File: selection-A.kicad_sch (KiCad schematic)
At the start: 3 parts, among them U0 SN74LS08N, U10 SN74LS08N, U13 SN74LVC1G32DBVR

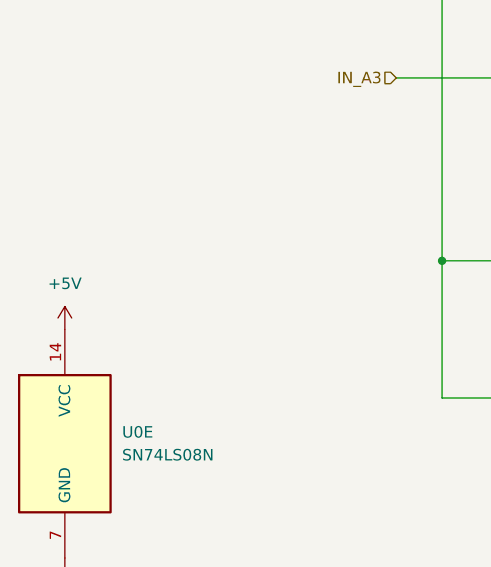
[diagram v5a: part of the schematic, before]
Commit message: feat: added capacitor with footprint
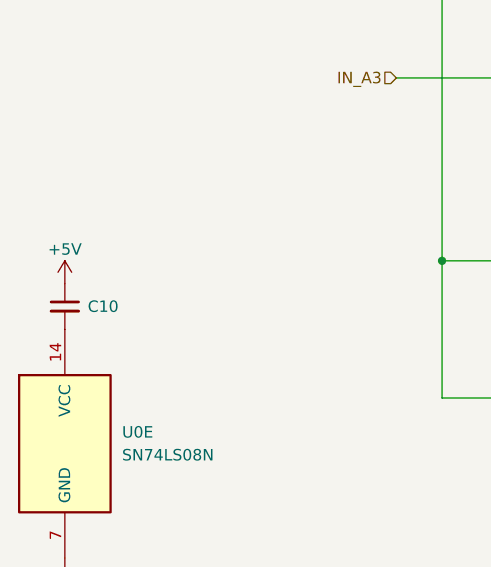
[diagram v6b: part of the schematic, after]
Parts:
- added C10: C_Small, Capacitor_SMD:C_0603_1608Metric_Pad1.08x0.95mm_HandSolder, symbol Device:C_Small
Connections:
- net +5V: now also C10.1; no longer U0.14 (VCC)
- new net: C10.2, U0.14 (VCC)
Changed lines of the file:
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@@
+	)
+	(symbol
+		(lib_id "Device:C_Small")
+		(at 54.61 127 0)
+		(unit 1)
+		(body_style 1)
+		(exclude_from_sim no)
+		(in_bom yes)
+		(on_board yes)
+		(in_pos_files yes)
+		(dnp no)
+		(fields_autoplaced yes)
+		(property "Reference" "C10"
+			(at 57.15 127.0062 0)
+			(show_name no)
+			(do_not_autoplace no)
+			(effects
+				(font
+					(size 1.27 1.27)
+				)
+				(justify left)
+			)
+		)
+		(property "Value" "C_Small"
+			(at 57.15 128.2762 0)
+			(hide yes)
+			(show_name no)
+			(do_not_autoplace no)
+			(effects
+				(font
+					(size 1.27 1.27)
+				)
+				(justify left)
+			)
+		)
+		(property "Footprint" "Capacitor_SMD:C_0603_1608Metric_Pad1.08x0.95mm_HandSolder"
+			(at 54.61 127 0)
+			(hide yes)
+			(show_name no)
+			(do_not_autoplace no)
+			(effects
+				(font
+					(size 1.27 1.27)
+				)
+			)
+		)
+		(property "Datasheet" ""
+			(at 54.61 127 0)
+			(hide yes)
+			(show_name no)
+			(do_not_autoplace no)
+			(effects
+				(font
+					(size 1.27 1.27)
+				)
+			)
+		)
+		(property "Description" "Unpolarized capacitor, small symbol"
+			(at 54.61 127 0)
+			(hide yes)
+			(show_name no)
+			(do_not_autoplace no)
+			(effects
+				(font
+					(size 1.27 1.27)
+				)
+			)
+		)
+		(pin "2"
+		)
+		(pin "1"
+		)
+		(instances
+			(project "alu"
+				(path "/4987240f-8890-46b8-b8e9-0d60580cb205/30c1ae8d-c878-40aa-ace0-371f489a4d3c"
+					(reference "C10")
+					(unit 1)
+				)
+			)
+		)
 	)
 	(symbol
@@
 	)
 	(symbol
+		(lib_id "power:+5V")
+		(at 54.61 124.46 0)
+		(unit 1)
+		(body_style 1)
+		(exclude_from_sim no)
+		(in_bom yes)
+		(on_board yes)
+		(in_pos_files yes)
+		(dnp no)
+		(property "Reference" "#PWR040"
+			(at 54.61 128.27 0)
+			(hide yes)
+			(show_name no)
+			(do_not_autoplace no)
+			(effects
+				(font
+					(size 1.27 1.27)
+				)
+			)
+		)
+		(property "Value" "+5V"
+			(at 54.61 120.65 0)
+			(show_name no)
+			(do_not_autoplace no)
+			(effects
+				(font
+					(size 1.27 1.27)
+				)
+			)
+		)
+		(property "Footprint" ""
+			(at 54.61 124.46 0)
+			(hide yes)
+			(show_name no)
+			(do_not_autoplace no)
+			(effects
+				(font
+					(size 1.27 1.27)
+				)
+			)
+		)
+		(property "Datasheet" ""
+			(at 54.61 124.46 0)
+			(hide yes)
+			(show_name no)
+			(do_not_autoplace no)
+			(effects
+				(font
+					(size 1.27 1.27)
+				)
+			)
+		)
+		(property "Description" "Power symbol creates a global label with name \"+5V\""
+			(at 54.61 124.46 0)
+			(hide yes)
+			(show_name no)
+			(do_not_autoplace no)
+			(effects
+				(font
+					(size 1.27 1.27)
+				)
+			)
+		)
+		(pin "1"
+		)
+		(instances
+			(project "alu"
+				(path "/4987240f-8890-46b8-b8e9-0d60580cb205/30c1ae8d-c878-40aa-ace0-371f489a4d3c"
+					(reference "#PWR040")
+					(unit 1)
+				)
+			)
+		)
+	)
+	(symbol
 		(lib_id "74xx:74LS08")
 		(at 54.61 142.24 0)
@@
 				)
 			)
-		)
-	)
-	(symbol
-		(lib_id "power:+5V")
-		(at 54.61 129.54 0)
-		(unit 1)
-		(body_style 1)
-		(exclude_from_sim no)
-		(in_bom yes)
-		(on_board yes)
-		(in_pos_files yes)
-		(dnp no)
-		(fields_autoplaced yes)
-		(property "Reference" "#PWR05"
-			(at 54.61 133.35 0)
-			(hide yes)
-			(show_name no)
-			(do_not_autoplace no)
-			(effects
-				(font
-					(size 1.27 1.27)
-				)
-			)
-		)
-		(property "Value" "+5V"
-			(at 54.61 124.46 0)
-			(show_name no)
-			(do_not_autoplace no)
-			(effects
-				(font
-					(size 1.27 1.27)
-				)
-			)
-		)
-		(property "Footprint" ""
-			(at 54.61 129.54 0)
-			(hide yes)
-			(show_name no)
-			(do_not_autoplace no)
-			(effects
-				(font
-					(size 1.27 1.27)
-				)
-			)
-		)
-		(property "Datasheet" ""
-			(at 54.61 129.54 0)
-			(hide yes)
-			(show_name no)
-			(do_not_autoplace no)
-			(effects
-				(font
-					(size 1.27 1.27)
-				)
-			)
-		)
-		(property "Description" "Power symbol creates a global label with name \"+5V\""
-			(at 54.61 129.54 0)
-			(hide yes)
-			(show_name no)
-			(do_not_autoplace no)
-			(effects
-				(font
-					(size 1.27 1.27)
-				)
-			)
-		)
-		(pin "1"
-		)
-		(instances
-			(project "alu"
-				(path "/4987240f-8890-46b8-b8e9-0d60580cb205/30c1ae8d-c878-40aa-ace0-371f489a4d3c"
-					(reference "#PWR05")
-					(unit 1)
-				)
-			)

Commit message: fix: merge
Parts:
- renumbered U13 to U10, U0 to U7, U10 to U9, U0 to U9
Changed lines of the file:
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@@
 		(dnp no)
 		(fields_autoplaced yes)
-		(property "Reference" "U13"
+		(property "Reference" "U10"
 			(at 124.46 34.2198 0)
 			(show_name no)
@@
 			(project "alu"
 				(path "/4987240f-8890-46b8-b8e9-0d60580cb205/30c1ae8d-c878-40aa-ace0-371f489a4d3c"
-					(reference "U13")
+					(reference "U10")
 					(unit 1)
 				)
@@
 		(dnp no)
 		(fields_autoplaced yes)
-		(property "Reference" "U0"
+		(property "Reference" "U7"
 			(at 135.8817 67.31 0)
 			(show_name no)
@@
 			(project "alu"
 				(path "/4987240f-8890-46b8-b8e9-0d60580cb205/30c1ae8d-c878-40aa-ace0-371f489a4d3c"
-					(reference "U0")
+					(reference "U7")
 					(unit 2)
 				)
@@
 		(dnp no)
 		(fields_autoplaced yes)
-		(property "Reference" "U10"
+		(property "Reference" "U9"
 			(at 135.8817 110.49 0)
 			(show_name no)
@@
 			(project "alu"
 				(path "/4987240f-8890-46b8-b8e9-0d60580cb205/30c1ae8d-c878-40aa-ace0-371f489a4d3c"
-					(reference "U10")
+					(reference "U9")
 					(unit 1)
 				)
@@
 		(dnp no)
 		(fields_autoplaced yes)
-		(property "Reference" "#PWR027"
+		(property "Reference" "#PWR?"
 			(at 111.76 34.29 0)
 			(hide yes)
@@
 			(project "alu"
 				(path "/4987240f-8890-46b8-b8e9-0d60580cb205/30c1ae8d-c878-40aa-ace0-371f489a4d3c"
-					(reference "#PWR027")
+					(reference "#PWR?")
 					(unit 1)
 				)
@@
 		(dnp no)
 		(fields_autoplaced yes)
-		(property "Reference" "#PWR07"
+		(property "Reference" "#PWR?"
 			(at 54.61 161.29 0)
 			(hide yes)
@@
 			(project "alu"
 				(path "/4987240f-8890-46b8-b8e9-0d60580cb205/30c1ae8d-c878-40aa-ace0-371f489a4d3c"
-					(reference "#PWR07")
+					(reference "#PWR?")
 					(unit 1)
 				)
@@
 		(dnp no)
 		(fields_autoplaced yes)
-		(property "Reference" "U10"
+		(property "Reference" "U9"
 			(at 135.8817 125.73 0)
 			(show_name no)
@@
 			(project "alu"
 				(path "/4987240f-8890-46b8-b8e9-0d60580cb205/30c1ae8d-c878-40aa-ace0-371f489a4d3c"
-					(reference "U10")
+					(reference "U9")
 					(unit 2)
 				)
@@
 		(dnp no)
 		(fields_autoplaced yes)
-		(property "Reference" "#PWR026"
+		(property "Reference" "#PWR?"
 			(at 111.76 57.15 0)
 			(hide yes)
@@
 			(project "alu"
 				(path "/4987240f-8890-46b8-b8e9-0d60580cb205/30c1ae8d-c878-40aa-ace0-371f489a4d3c"
-					(reference "#PWR026")
+					(reference "#PWR?")
 					(unit 1)
 				)
@@
 		(dnp no)
 		(fields_autoplaced yes)
-		(property "Reference" "U0"
+		(property "Reference" "U7"
 			(at 135.8817 95.25 0)
 			(show_name no)
@@
 			(project "alu"
 				(path "/4987240f-8890-46b8-b8e9-0d60580cb205/30c1ae8d-c878-40aa-ace0-371f489a4d3c"
-					(reference "U0")
+					(reference "U7")
 					(unit 4)
 				)
@@
 		(in_pos_files yes)
 		(dnp no)
-		(property "Reference" "#PWR040"
+		(property "Reference" "#PWR?"
 			(at 54.61 128.27 0)
 			(hide yes)
@@
 			(project "alu"
 				(path "/4987240f-8890-46b8-b8e9-0d60580cb205/30c1ae8d-c878-40aa-ace0-371f489a4d3c"
-					(reference "#PWR040")
+					(reference "#PWR?")
 					(unit 1)
 				)
@@
 		(dnp no)
 		(fields_autoplaced yes)
-		(property "Reference" "U0"
+		(property "Reference" "U9"
 			(at 60.96 140.9699 0)
 			(show_name no)
@@
 			(project "alu"
 				(path "/4987240f-8890-46b8-b8e9-0d60580cb205/30c1ae8d-c878-40aa-ace0-371f489a4d3c"
-					(reference "U0")
+					(reference "U9")
 					(unit 5)
 				)
@@
 		(dnp no)
 		(fields_autoplaced yes)
-		(property "Reference" "U0"
+		(property "Reference" "U7"
 			(at 135.8817 53.34 0)
 			(show_name no)
@@
 			(project "alu"
 				(path "/4987240f-8890-46b8-b8e9-0d60580cb205/30c1ae8d-c878-40aa-ace0-371f489a4d3c"
-					(reference "U0")
+					(reference "U7")
 					(unit 1)
 				)
@@
 		(dnp no)
 		(fields_autoplaced yes)
-		(property "Reference" "U0"
+		(property "Reference" "U7"
 			(at 135.8817 81.28 0)
 			(show_name no)
@@
 			(project "alu"
 				(path "/4987240f-8890-46b8-b8e9-0d60580cb205/30c1ae8d-c878-40aa-ace0-371f489a4d3c"
-					(reference "U0")
+					(reference "U7")
 					(unit 3)
 				)

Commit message: fix: fixed capa
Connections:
- net +5V: now also U9.14 (VCC)
- net at C10.2: no longer U9.14 (VCC)
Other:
- moved on the sheet: C10
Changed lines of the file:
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@@
+	)
+	(junction
+		(at 54.61 129.54)
+		(diameter 0)
+		(color 0 0 0 0)
 	)
 	(junction
@@
 	(wire
 		(pts
+			(xy 54.61 129.54) (xy 43.18 129.54)
+		)
+		(stroke
+			(width 0)
+			(type default)
+		)
+	)
+	(wire
+		(pts
 			(xy 91.44 43.18) (xy 96.52 43.18)
 		)
@@
 	(wire
 		(pts
+			(xy 54.61 153.67) (xy 43.18 153.67)
+		)
+		(stroke
+			(width 0)
+			(type default)
+		)
+	)
+	(wire
+		(pts
 			(xy 124.46 106.68) (xy 128.27 106.68)
 		)
@@
 	(wire
 		(pts
+			(xy 43.18 129.54) (xy 43.18 139.7)
+		)
+		(stroke
+			(width 0)
+			(type default)
+		)
+	)
+	(wire
+		(pts
 			(xy 128.27 132.08) (xy 111.76 132.08)
+		)
+		(stroke
+			(width 0)
+			(type default)
+		)
+	)
+	(wire
+		(pts
+			(xy 43.18 153.67) (xy 43.18 144.78)
 		)
 		(stroke
@@
 	(symbol
 		(lib_id "Device:C_Small")
-		(at 54.61 127 0)
+		(at 43.18 142.24 0)
 		(unit 1)
 		(body_style 1)
@@
 		(fields_autoplaced yes)
 		(property "Reference" "C10"
-			(at 57.15 127.0062 0)
+			(at 45.72 142.2462 0)
 			(show_name no)
 			(do_not_autoplace no)
@@
 		)
 		(property "Value" "C_Small"
-			(at 57.15 128.2762 0)
+			(at 45.72 143.5162 0)
 			(hide yes)
 			(show_name no)
@@
 		)
 		(property "Footprint" "Capacitor_SMD:C_0603_1608Metric_Pad1.08x0.95mm_HandSolder"
-			(at 54.61 127 0)
+			(at 43.18 142.24 0)
 			(hide yes)
 			(show_name no)
@@
 		)
 		(property "Datasheet" ""
-			(at 54.61 127 0)
+			(at 43.18 142.24 0)
 			(hide yes)
 			(show_name no)
@@
 		)
 		(property "Description" "Unpolarized capacitor, small symbol"
-			(at 54.61 127 0)
+			(at 43.18 142.24 0)
 			(hide yes)
 			(show_name no)
@@
 	(symbol
 		(lib_id "power:+5V")
-		(at 54.61 124.46 0)
+		(at 54.61 129.54 0)
 		(unit 1)
 		(body_style 1)
@@
 		(dnp no)
 		(property "Reference" "#PWR?"
-			(at 54.61 128.27 0)
+			(at 54.61 133.35 0)
 			(hide yes)
 			(show_name no)
@@
 		)
 		(property "Value" "+5V"
-			(at 54.61 120.65 0)
+			(at 54.61 125.73 0)
 			(show_name no)
 			(do_not_autoplace no)
@@
 		)
 		(property "Footprint" ""
-			(at 54.61 124.46 0)
+			(at 54.61 129.54 0)
 			(hide yes)
 			(show_name no)
@@
 		)
 		(property "Datasheet" ""
-			(at 54.61 124.46 0)
+			(at 54.61 129.54 0)
 			(hide yes)
 			(show_name no)
@@
 		)
 		(property "Description" "Power symbol creates a global label with name \"+5V\""
-			(at 54.61 124.46 0)
-			(hide yes)
-			(show_name no)
+			(at 54.61 129.54 0)
+			(hide yes)
+			(show_name no)
